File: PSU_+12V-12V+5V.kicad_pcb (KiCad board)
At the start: 2 copper layers, 97.2 x 102.2 mm, 61 parts, among them J1 PSU12a, J2 PSU12b, J3 PSU5, J4 230V, Q1 BC557, Q2 BC557, Q3 BC547, Q4 BC547, U1 LM317L, U2 LM317L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

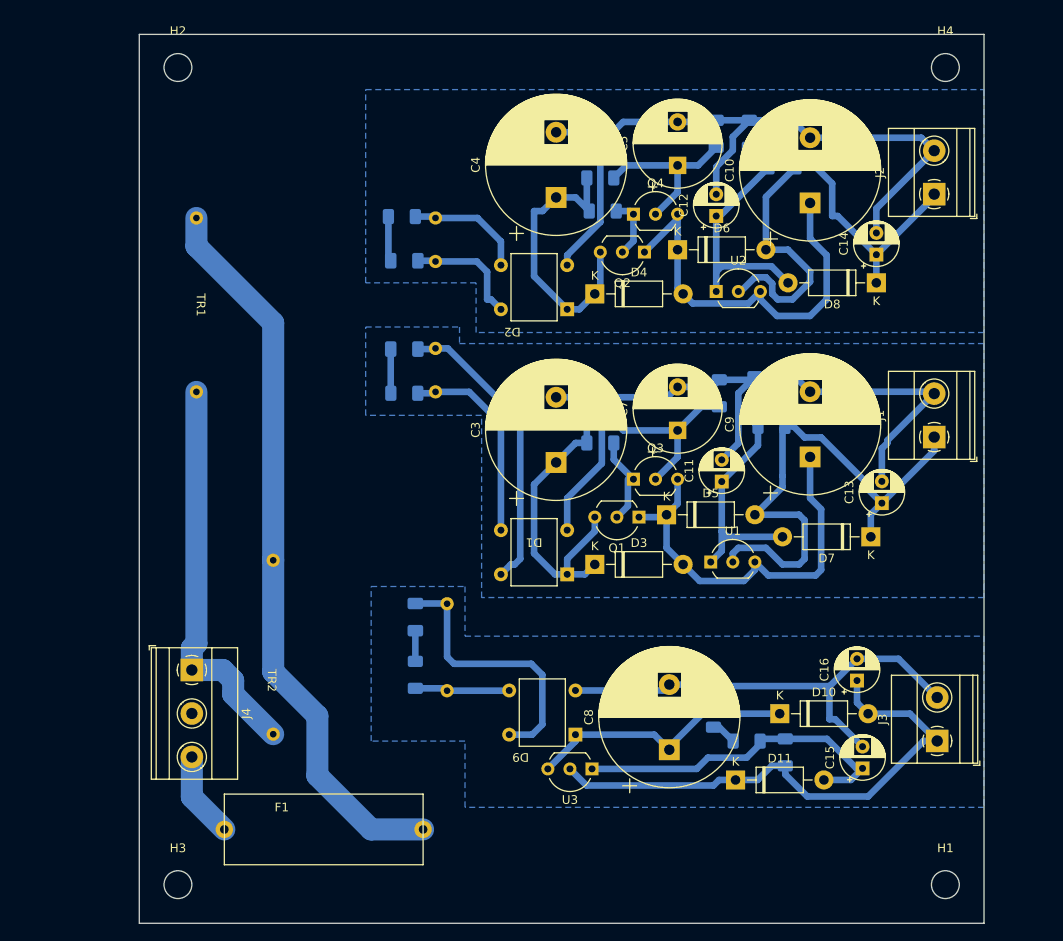
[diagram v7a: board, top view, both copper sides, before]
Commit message: Changed type capacitor
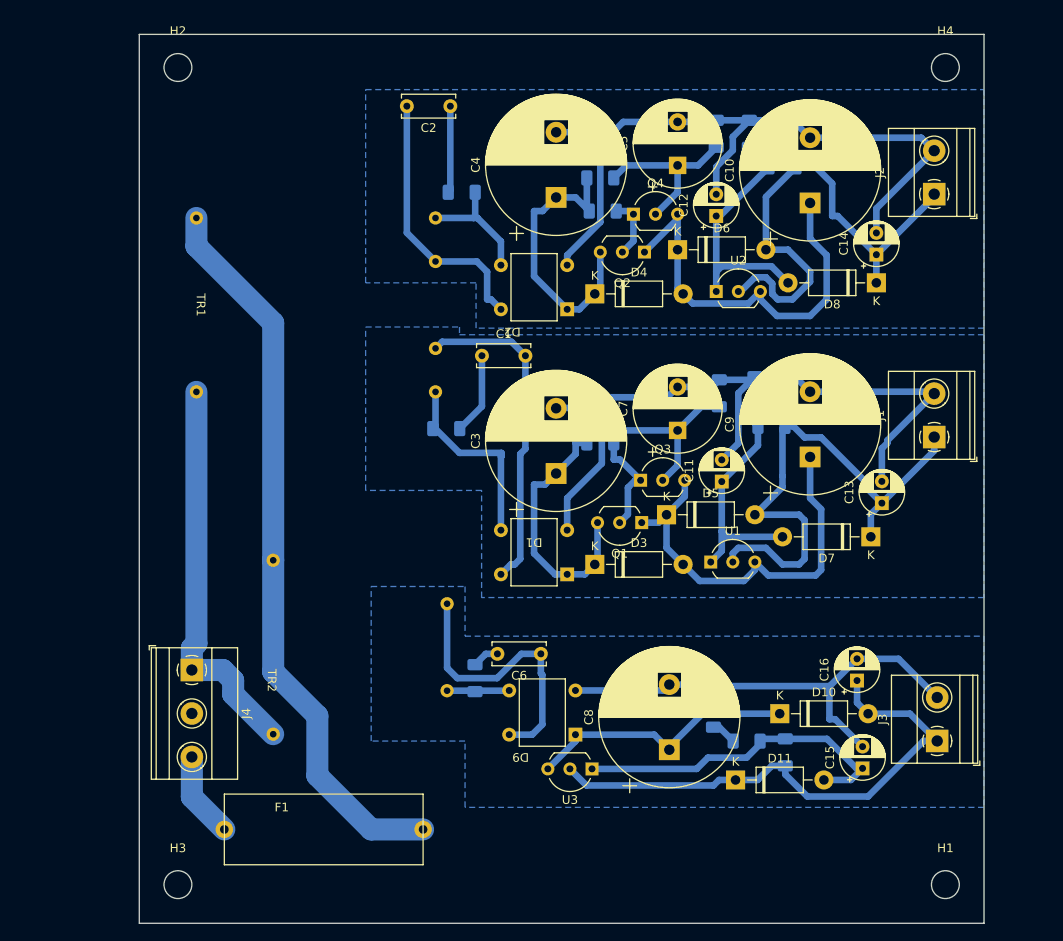
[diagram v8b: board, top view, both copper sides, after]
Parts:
- C1, C2, C6: footprint Capacitor_SMD:C_1206_3216Metric_Pad1.33x1.80mm_HandSolder -> Capacitor_THT:C_Disc_D6.0mm_W2.5mm_P5.00mm; moved to F.Cu
- moved C2 18.6 mm to (86.6, 48.3), turned to 180 degrees
- moved C6 15.0 mm to (97.0, 111.3), turned to 180 degrees
- moved C1 8.96 mm to (90.2, 77.0)
- moved R2 7.43 mm to (87.9, 58.2)
- moved R8 6.87 mm to (89.4, 114.0)
- moved R1 6.31 mm to (86.1, 85.3), turned to 0 degrees
- moved C3 1.27 mm to (98.7, 90.5)
- moved Q3 0.84 mm to (108.5, 91.3)
- moved Q1 0.71 mm to (108.6, 96.2)
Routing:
- net Net-(C2-Pad2): track 13.7 -> 30.9 mm
- net Net-(C2-Pad1): track 5.19 -> 10.0 mm
- net Net-(C1-Pad1): track 5.09 -> 9.44 mm
- net Net-(C1-Pad2): track 34.1 -> 37.9 mm
- net Net-(D9-Pad3): track 10.9 -> 7.16 mm
- net Net-(Q1-Pad2): track 9.99 -> 12.2 mm
- net Net-(C3-Pad1): track 34.9 -> 32.6 mm
- net Net-(D1-Pad3): track 23.4 -> 22.3 mm
- net Net-(C6-Pad1): track 31.6 -> 32.3 mm
- net Net-(D2-Pad3): track 13.8 -> 14.4 mm
